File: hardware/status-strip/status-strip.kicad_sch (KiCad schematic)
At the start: 13 parts, among them J1 Conn_01x03

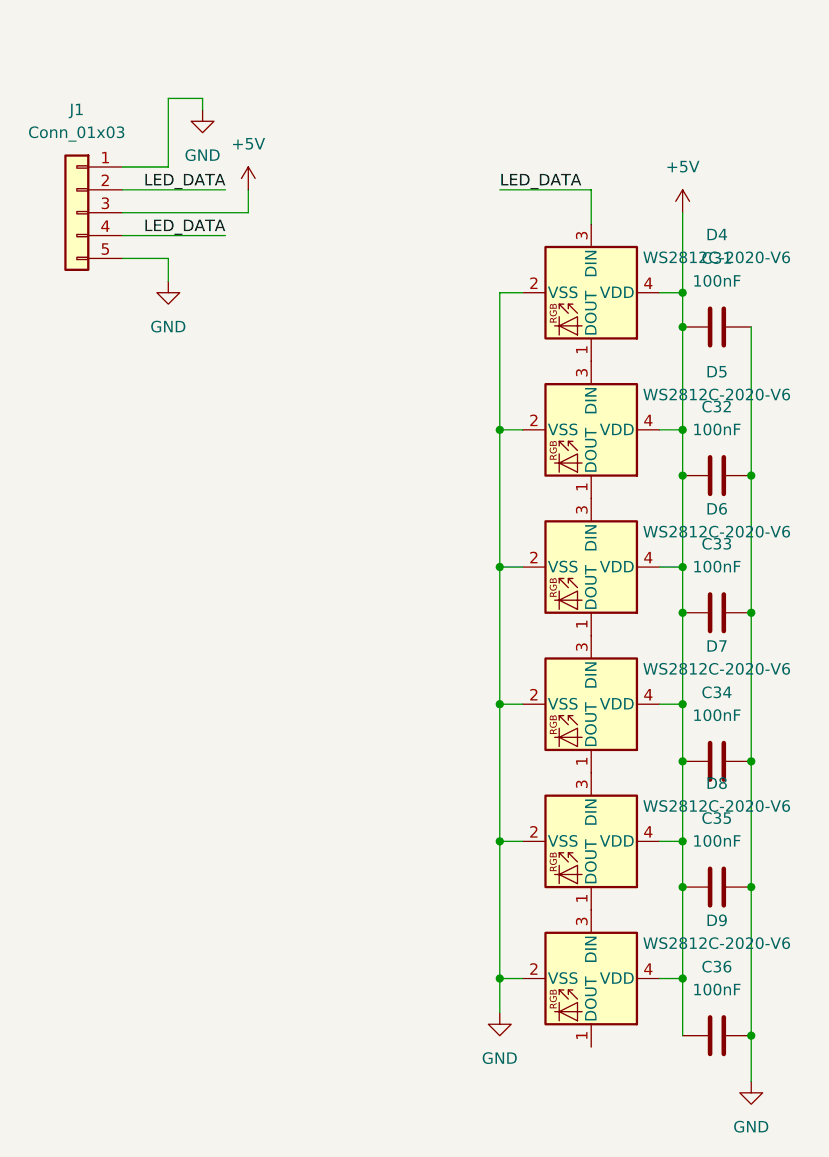
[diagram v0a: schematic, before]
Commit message: feat(status-strip): add system-level status led
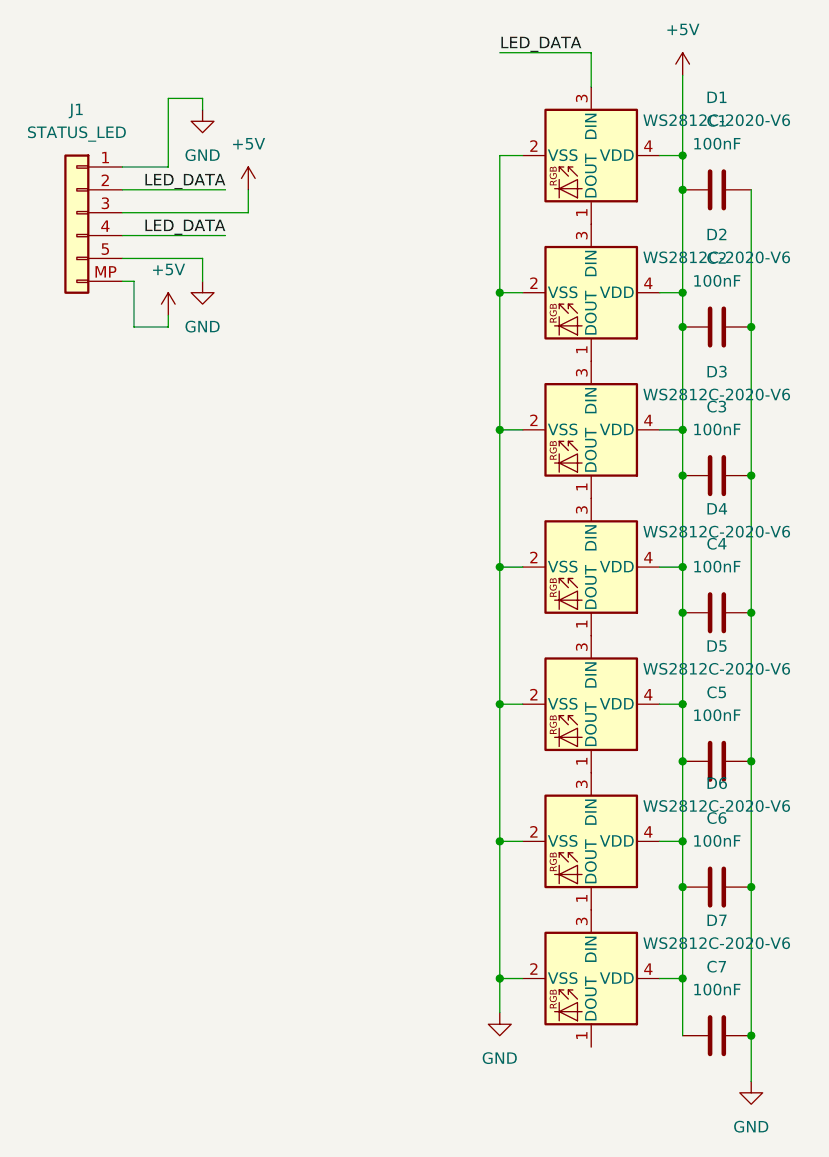
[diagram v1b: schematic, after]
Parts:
- added C2: 100nF, Local Library:C_0402_1005Metric, symbol Device:C
- added D2: WS2812C-2020-V6, Local Library:LED_WS2812B-2020_PLCC4_2.0x2.0mm, symbol LED:WS2812B-2020
- J1: value Conn_01x03 -> STATUS_LED; symbol Connector_Generic:Conn_01x05 -> Connector_Generic:Conn_01x06
- renumbered C31 to C1, C32 to C3, C33 to C4, C34 to C5, C35 to C6, C36 to C7, D4 to D1, D5 to D3, D6 to D4, D7 to D5, D8 to D6, D9 to D7
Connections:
- net +5V: now also J1.MP (Pin_6), C2.1, D2.4 (VDD)
- net GND: now also C2.2, D2.2 (VSS)
- net at D1.1 (DOUT): now also D2.3 (DIN); no longer D3.3 (DIN)
- new net: D2.1 (DOUT), D3.3 (DIN)
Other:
- title: (none) -> Status Strip
- moved on the sheet: C1, D1
